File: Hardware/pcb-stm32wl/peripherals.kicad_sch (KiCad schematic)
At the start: 35 parts, among them J10 Qwiic, J11 Conn_02x08_Odd_Even, J13 Conn_02x08_Odd_Even, J8 DEBUG, J9 UART/I2C, SW1 USR_BTN, SW2 RESET, U3 AD7124-8BCPZ-RL7, U6 ICM-45605, U7 MRF89XAM9AT-I/RM

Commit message: review session 2
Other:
- note added: "Add in capacitor"
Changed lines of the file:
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@@
 	(rectangle
 		(start 172.974 76.962)
-		(end 282.956 130.556)
+		(end 282.956 130.048)
 		(stroke
 			(width 0.508)
@@
 		(fill
 			(type none)
+		)
+	)
+	(text "Add in capacitor"
+		(exclude_from_sim no)
+		(at 34.544 111.76 0)
+		(effects
+			(font
+				(size 1.4986 1.4986)
+				(color 0 255 0 1)
+			)
 		)
 	)
@@
 				(size 1.4986 1.4986)
 				(color 194 0 0 1)
+			)
+		)
+	)
+	(text "Add in capacitor"
+		(exclude_from_sim no)
+		(at -6.604 38.862 0)
+		(effects
+			(font
+				(size 1.4986 1.4986)
+				(color 0 255 0 1)
 			)
 		)
@@
 		)
 	)
+	(text "Add in capacitor"
+		(exclude_from_sim no)
+		(at 113.03 108.204 0)
+		(effects
+			(font
+				(size 1.4986 1.4986)
+				(color 0 255 0 1)
+			)
+		)
+	)

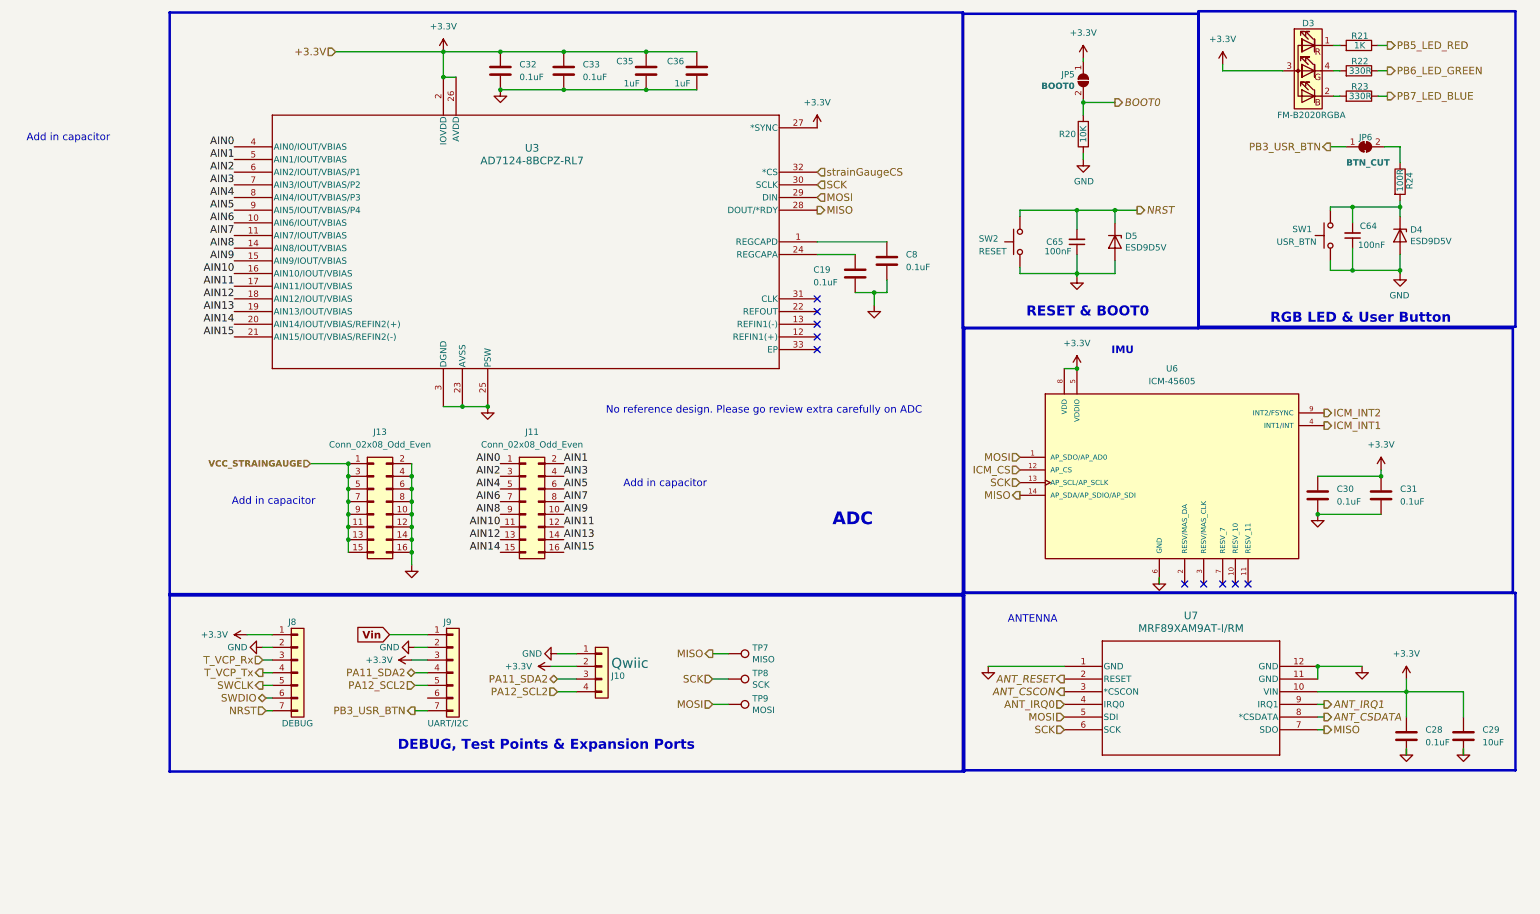
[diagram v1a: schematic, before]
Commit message: . Added NUCLEO reference schematics . Cleaned, renamed schematic pins for clarity . Fixed PMOS polarity bug . Added PMOS for switching StrainV . Added capacitors to AIN, StrainV . Cleaned git repository by removing backups, temporary lck files, ignoring KiCad cache files
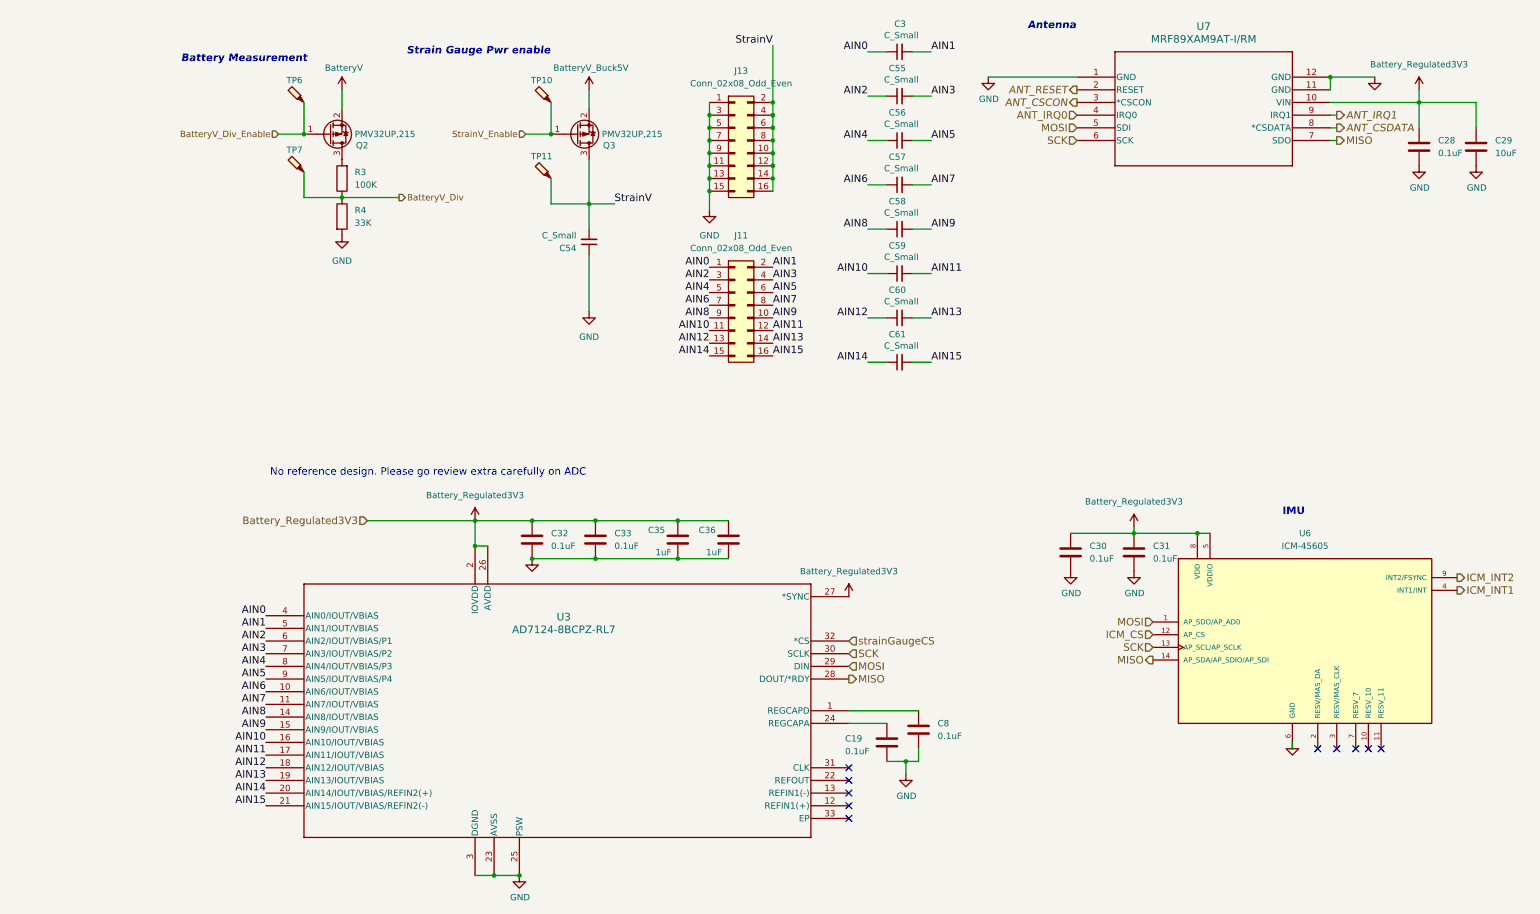
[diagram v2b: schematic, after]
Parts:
- removed C64, C65: 100nF, Capacitor_SMD:C_0402_1005Metric, symbol Device:C_Small
- removed D3: FM-B2020RGBA, LED_SMD:LED_Cree-PLCC4_2x2mm_CW, symbol node-lib-v1:FM-B2020RGBA
- removed D4, D5: ESD9D5V, Diode_SMD:D_SOD-923, symbol Device:D_Zener
- removed J10: Qwiic, Connector_JST:JST_SH_BM04B-SRSS-TB_1x04-1MP_P1.00mm_Vertical, symbol Connector_Generic:Conn_01x04
- removed J8: DEBUG, Connector_PinSocket_2.54mm:PinSocket_1x07_P2.54mm_Vertical, symbol Connector_Generic:Conn_01x07
- removed J9: UART/I2C, Connector_PinSocket_2.54mm:PinSocket_1x07_P2.54mm_Vertical, symbol Connector_Generic:Conn_01x07
- removed JP5: BOOT0, Connector_PinHeader_1.27mm:PinHeader_1x02_P1.27mm_Vertical, symbol Jumper:SolderJumper_2_Open
- removed JP6: BTN_CUT, Jumper:SolderJumper-2_P1.3mm_Bridged2Bar_RoundedPad1.0x1.5mm, symbol Jumper:SolderJumper_2_Bridged
- removed R20: 10K, Inductor_SMD:L_0402_1005Metric, symbol Device:R
- removed R21: 1K, Resistor_SMD:R_0402_1005Metric, symbol Device:R
- removed R22, R23: 330R, Resistor_SMD:R_0402_1005Metric, symbol Device:R
- removed R24: 100R, Resistor_SMD:R_0402_1005Metric, symbol Device:R
- removed SW1: USR_BTN, node-lib-v1:PushButton_KSC721GLFS, symbol Switch:SW_Push
- removed SW2: RESET, node-lib-v1:SW_SPST_SKSHABE010, symbol Switch:SW_Push
- removed TP7: MISO, TestPoint:TestPoint_Pad_D1.5mm, symbol Connector:TestPoint
- removed TP8: SCK, TestPoint:TestPoint_Pad_D1.5mm, symbol Connector:TestPoint
- removed TP9: MOSI, TestPoint:TestPoint_Pad_D1.5mm, symbol Connector:TestPoint
- added C3, C54, C55, C56, C57, C58, C59, C60, C61: C_Small, symbol Device:C_Small
- added Q2, Q3: PMV32UP,215, Package_TO_SOT_SMD:SOT-23, symbol Device:Q_PMOS_GSD
- added R3: 100K, symbol Device:R
- added R4: 33K, symbol Device:R
- added TP10, TP11, TP6, TP7: VBattery_Div_Enable, TestPoint:TestPoint_Pad_D1.5mm, symbol Connector:TestPoint_Probe
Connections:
- net VCC_STRAINGAUGE is gone; now on net GND: J13.1 (Pin_1), J13.11 (Pin_11), J13.13 (Pin_13), J13.15 (Pin_15), J13.3 (Pin_3), J13.5 (Pin_5), J13.7 (Pin_7), J13.9 (Pin_9)
- net AIN0: now also C3.1
- net AIN1: now also C3.2
- net AIN10: now also C59.1
- net AIN11: now also C59.2
- net AIN12: now also C60.1
- net AIN13: now also C60.2
- net AIN14: now also C61.1
- net AIN15: now also C61.2
- net AIN2: now also C55.1
- net AIN3: now also C55.2
- net AIN4: now also C56.1
- net AIN5: now also C56.2
- net AIN6: now also C57.1
- net AIN7: now also C57.2
- net AIN8: now also C58.1
- net AIN9: now also C58.2
- net GND: now also C54.1, R4.2; no longer J13.10 (Pin_10), J13.12 (Pin_12), J13.14 (Pin_14), J13.16 (Pin_16), J13.2 (Pin_2), J13.4 (Pin_4), J13.6 (Pin_6), J13.8 (Pin_8)
- net +3.3V renamed Battery_Regulated3V3
- new net: Q2.3 (D), R3.2
- new net BatteryV: Q2.2 (S)
- new net BatteryV_Buck5V: Q3.2 (S)
- new net BatteryV_Div: R3.1, R4.1, TP7.1
- new net BatteryV_Div_Enable: Q2.1 (G), TP6.1
- new net StrainV: C54.2, J13.10 (Pin_10), J13.12 (Pin_12), J13.14 (Pin_14), J13.16 (Pin_16), J13.2 (Pin_2), J13.4 (Pin_4), J13.6 (Pin_6), J13.8 (Pin_8), Q3.3 (D), TP11.1
- new net StrainV_Enable: Q3.1 (G), TP10.1
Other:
- note added: "Antenna"
- note added: "Battery Measurement"
- note added: "Strain Gauge Pwr enable"
- note removed: "ADC"
- note removed: "ANTENNA"
- note removed: "Add in capacitor"
- note removed: "DEBUG, Test Points & Expansion Ports"
- note removed: "RESET & BOOT0"
- note removed: "RGB LED & User Button"
- moved on the sheet: C19, C28, C29, C30, C31, C32, C33, C35, C36, C8, J11, J13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

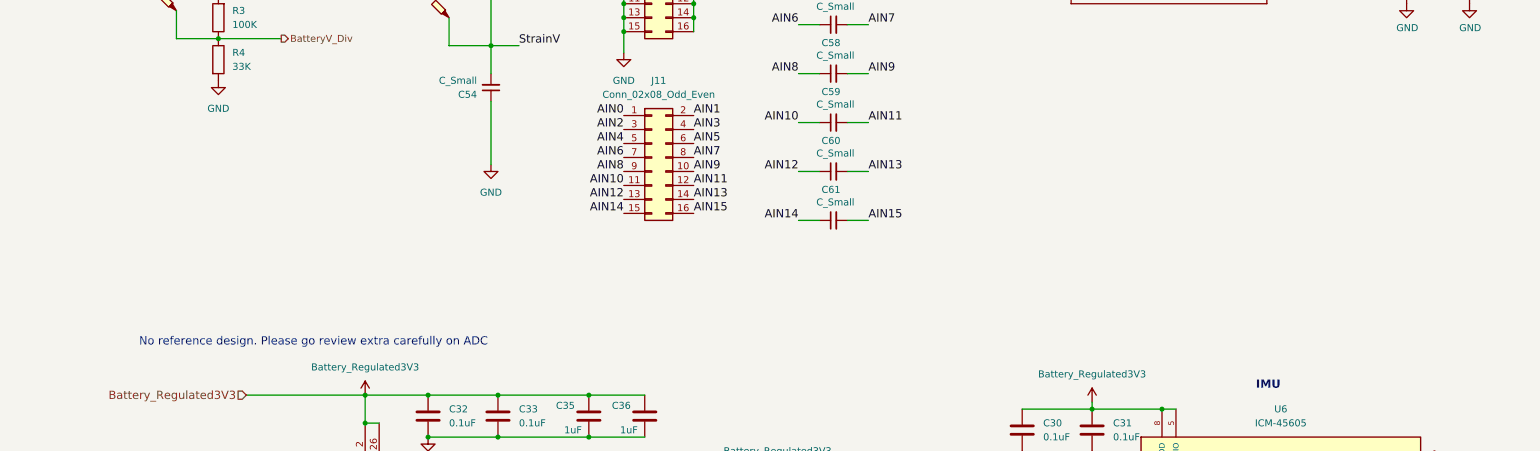
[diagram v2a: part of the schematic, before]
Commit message: Both mosfet will not be added into circuit. Both IMU and ANTENNA have sleep mode, which is in the micro to milliamp current usage range. Add in capacitor will optimize the system slighty, however the complexity of the problem is high. So I have opted to accept the uncertainty of the measurements.
Capacitor. Placement of capacitor is not accross differential. But we need 1 cap for each AIN, in addition to this, our switching frequency
will be varied significantly due to our battery range. This is very complicated stuff to size for. So in terms of time, it may be best to not add this in.
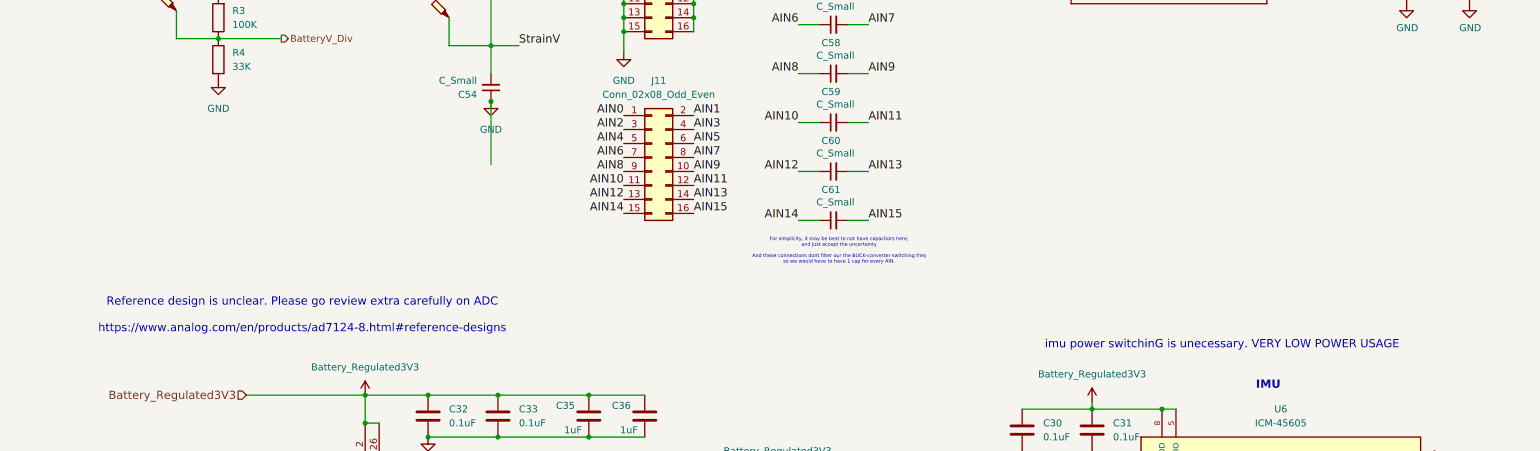
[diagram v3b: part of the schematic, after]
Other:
- note added: "For simplicity, it may be best to not have capacitors here, and just accept the uncertainty And these connections dont filter our the BUCK-converter switching freq so we would have to have 1 cap for every AIN."
- note added: "Reference design is unclear. Please go review extra carefully on ADC https://www.analog.com/en/products/ad7124-8.html#reference-designs"
- note added: "imu power switchinG is unecessary. VERY LOW POWER USAGE"
- note removed: "No reference design. Please go review extra carefully on ADC"
